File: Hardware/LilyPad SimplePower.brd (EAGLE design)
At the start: 27.9 x 27.9 mm, 20 parts, among them U1 MCP73831

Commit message: Adding review changes
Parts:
- added U$6: REVISION, SparkFun-Aesthetics:REVISION
- SJ1: value SOLDERJUMPERTRACE -> SOLDERJUMPERNC; device SparkFun-Passives:SJ_2S-TRACE -> SparkFun-Passives:SJ_2S
- U$1: value LOGO-LPL -> LOGO-LPLP; device LilyPad-Wearables:LOGO-L -> LilyPad-Wearables:LOGO-LILYPAD
- moved JP3 3.24 mm to (5.71, -4.13)
- moved U$5 3.17 mm to (-6.03, -2.54)
- moved S1 1.80 mm to (0.00, -2.54)
- moved C2 1.42 mm to (-6.35, -13.0)
- moved JP1 1.31 mm to (-9.84, -2.54)
- moved R4 1.27 mm to (-4.45, -13.0)
- moved U1 1.27 mm to (-5.71, -8.89)
- moved U$1 1.27 mm to (-0.64, 2.54), turned to 0 degrees
- moved C1 0.64 mm to (-1.27, -7.62)
- moved R3 0.64 mm to (1.27, -7.62)
- moved JP4 0.32 mm to (12.4, -2.54)
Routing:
- net N$2: track 6.13 -> 8.58 mm
- net N$4: track 16.3 -> 17.5 mm
- net N$5: track 3.41 -> 4.05 mm
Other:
- board size 27.9 x 27.9 mm -> 28.4 x 28.4 mm
- board text added: "NC"

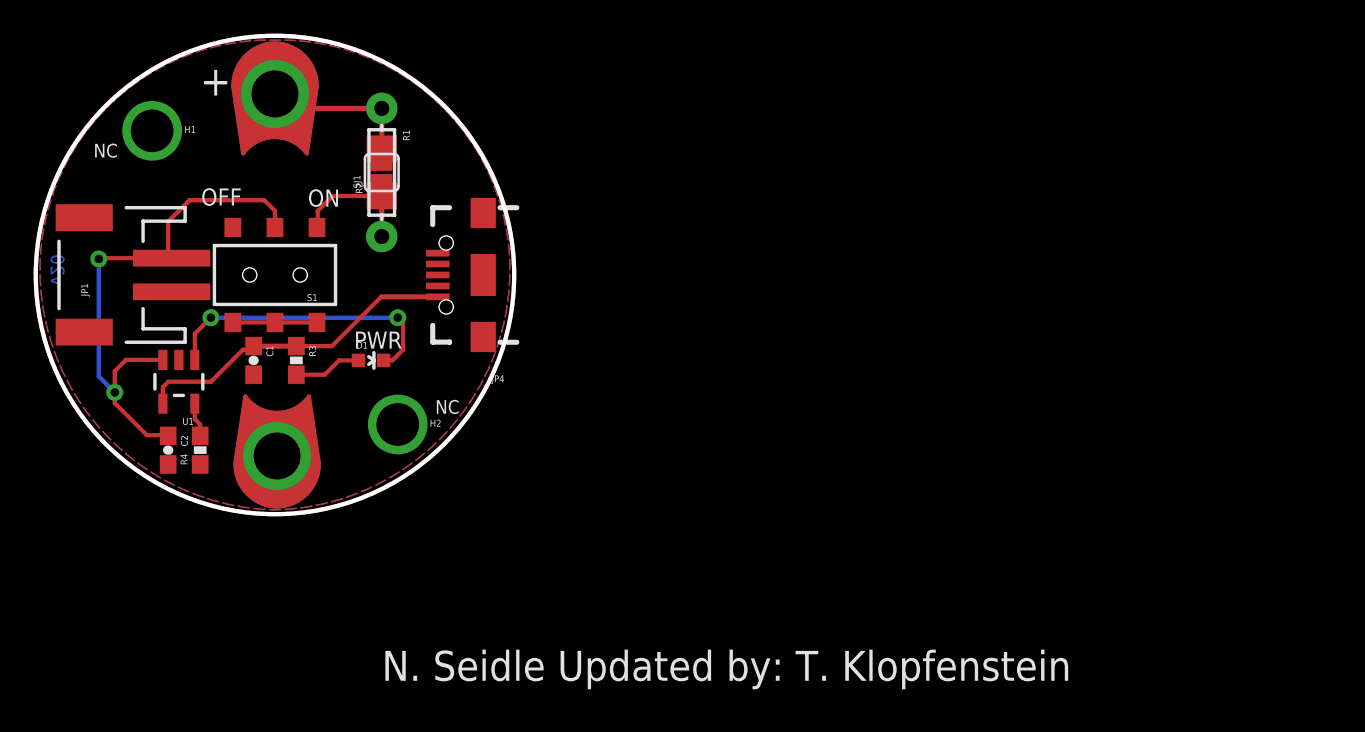
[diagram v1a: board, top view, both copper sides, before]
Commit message: Fixing PWR label to CHG on LED
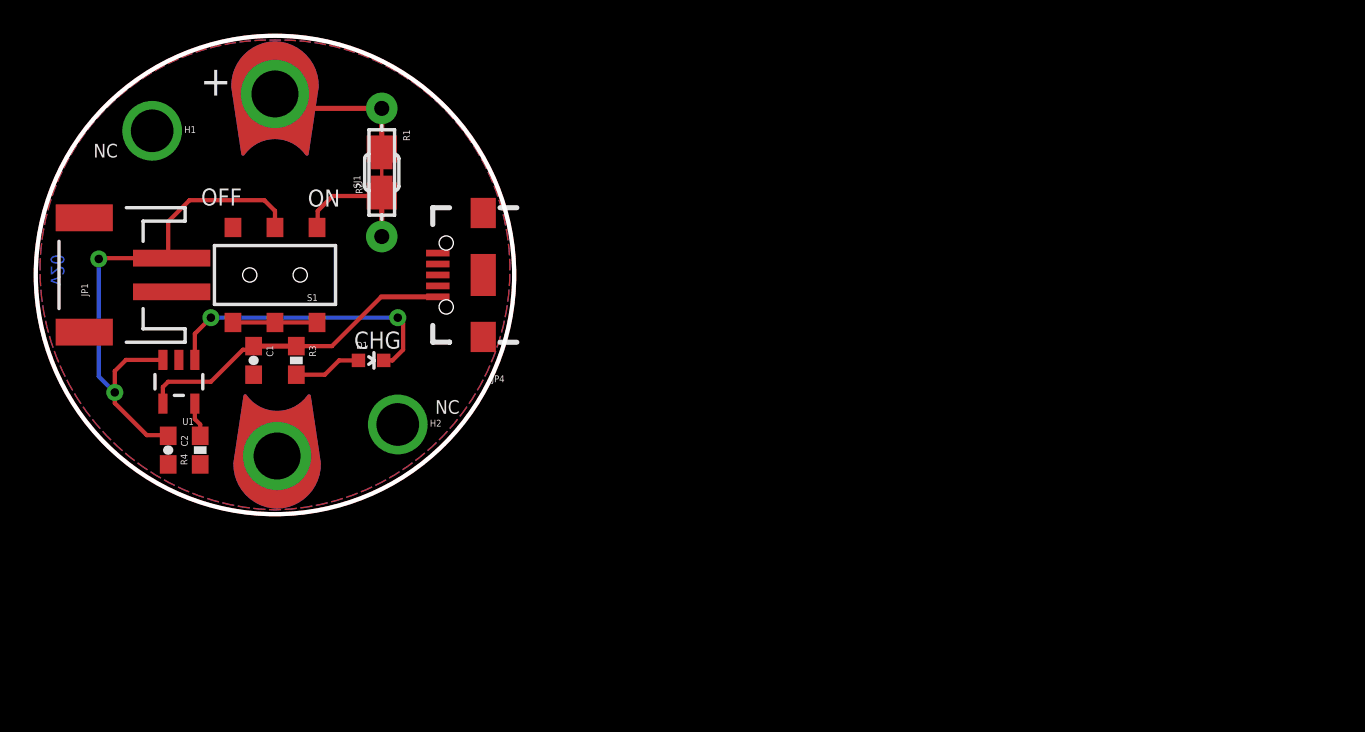
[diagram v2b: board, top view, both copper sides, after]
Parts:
- removed U$2: (no value), SparkFun-Aesthetics:CREATIVE_COMMONS
- added FRAME1: FRAME-LETTER, SparkFun-Aesthetics:CREATIVE_COMMONS
- SJ1: value SOLDERJUMPERNC -> SOLDERJUMPERTRACE; device SparkFun-Passives:SJ_2S -> SparkFun-Passives:SJ_2S-TRACE
- moved U$6 31.8 mm to (-12.7, -29.2)
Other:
- board text added: "CHG"
- board text added: "N. Seidle"
- board text added: "Toni Klopfenstein"
- board text removed: "N. Seidle Updated by: T. Klopfenstein"
- board text removed: "PWR"

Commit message: midway work  on updating design
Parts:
- removed R1: (no value), SparkFun:AXIAL-0.3
- removed R2: (no value), SparkFun:1206
- removed SJ1: SOLDERJUMPERTRACE, SparkFun-Passives:SJ_2S-TRACE
- added H3, H4: SEW_HOLE, LilyPad-Wearables:SIMPLE_HOLE
- moved H2 16.9 mm to (9.21, 5.40)
- moved C2 15.9 mm to (-1.65, 2.22), turned to 0 degrees
- moved U1 7.31 mm to (-1.59, -2.86)
- moved R4 7.17 mm to (-1.65, -6.35), turned to 0 degrees
- moved C1 4.80 mm to (-6.03, -8.26), turned to 180 degrees
- moved S1 4.13 mm to (4.13, -2.54), turned to 270 degrees
- moved R3 2.93 mm to (-1.59, -8.26), turned to 0 degrees
- moved D1 2.01 mm to (3.81, -8.26)
- moved H1 1.71 mm to (-8.89, 5.40)
- moved U$1 1.00 mm to (0.32, 2.22)
- moved JP1 0.32 mm to (-9.84, -2.86)
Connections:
- removed net +: R1.P$1, R2.2, SJ1.2, U$4.1
- removed net N$2: R1.P$2, R2.1, S1.4, SJ1.1
- removed net SINK2: S1.6
- new net N$6: S1.4, U$4.1
- net GND: now also S1.6
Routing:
- net N$1: track 32.1 -> 14.1 mm, vias 2 -> 0
- net +: track 10.0 -> 0.00 mm
- net N$6: track 0.00 -> 8.80 mm
- net N$2: track 8.48 -> 0.00 mm
- net N$4: track 17.5 -> 10.3 mm, vias 2 -> 0
- net N$3: track 19.6 -> 23.1 mm, vias 0 -> 2
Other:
- board text added: "-"

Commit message: More petal work
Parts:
- H1: value SEW_HOLE -> SEWTAP4; device LilyPad-Wearables:SIMPLE_HOLE -> LilyPad-Wearables:PETAL-SMALL
- H2, H3, H4: value SEW_HOLE -> SEWTAP6; device LilyPad-Wearables:SIMPLE_HOLE -> LilyPad-Wearables:PETAL-SMALL-2SIDE
- moved D1 2.31 mm to (1.59, -7.62), turned to 0 degrees
- moved C1 1.14 mm to (-6.99, -7.62)
- moved H3 1.14 mm to (8.57, -11.1), turned to 45 degrees
- moved H4 1.14 mm to (-8.57, -11.1), turned to 315 degrees
- moved H2 0.90 mm to (8.57, 6.03), turned to 135 degrees
- moved H1 0.71 mm to (-8.57, 6.03), turned to 225 degrees
- moved R3 0.64 mm to (-1.59, -7.62)
- moved R4 0.63 mm to (-1.65, -5.71)
- moved JP1 0.32 mm to (-9.84, -2.54)
- moved U1 0.32 mm to (-1.59, -2.54)
- moved U$3 0.17 mm to (-0.04, -13.4)
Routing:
- net N$3: track 23.1 -> 27.3 mm
- net N$5: track 3.80 -> 2.64 mm
- net N$4: track 10.3 -> 9.35 mm
- net N$1: track 14.1 -> 13.6 mm

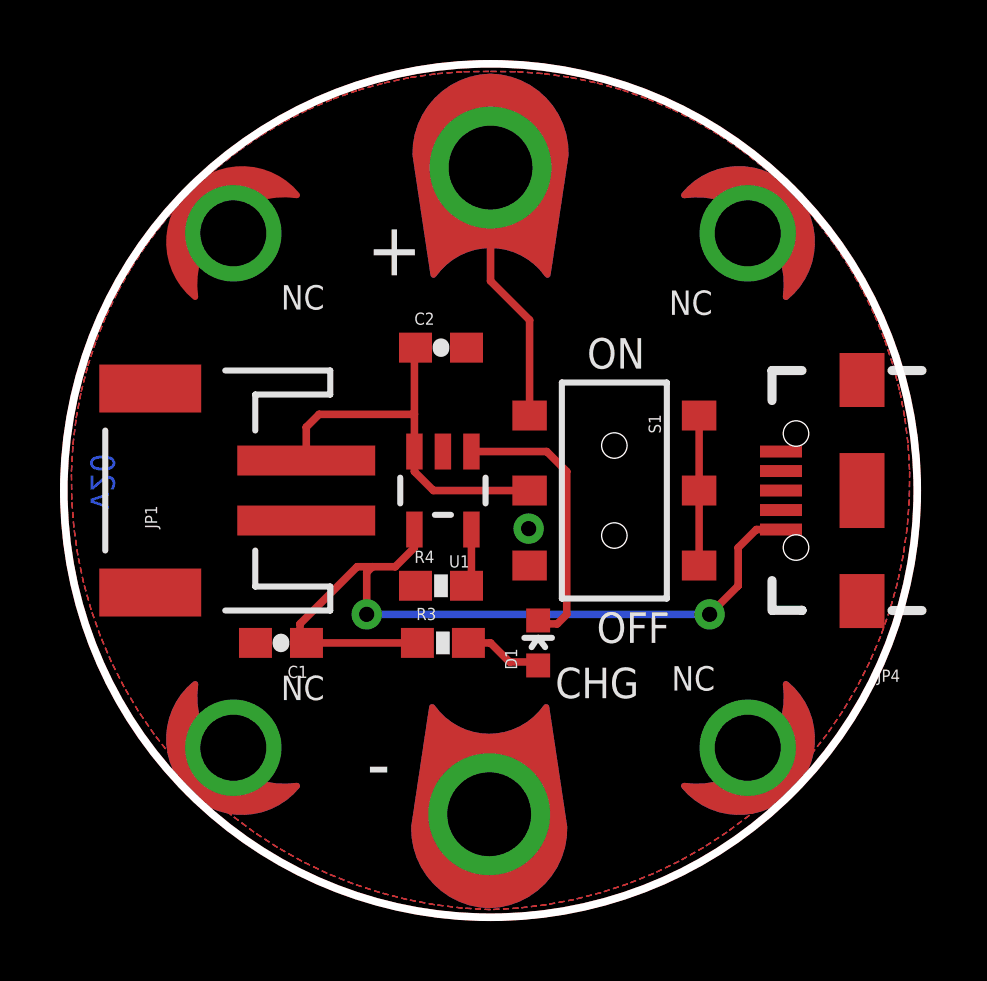
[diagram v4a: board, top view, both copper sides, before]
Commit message: Initial polygon pours corrected
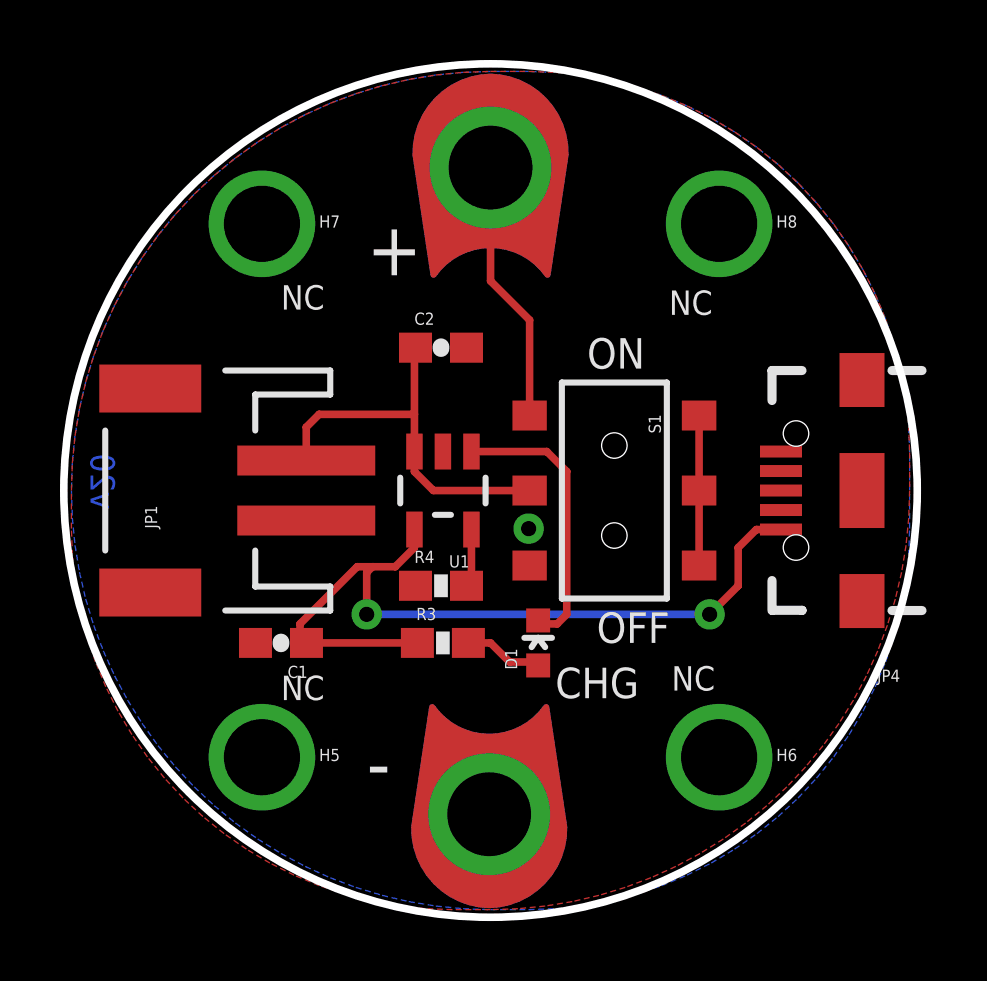
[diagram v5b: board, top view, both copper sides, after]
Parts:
- removed H1: SEWTAP4, LilyPad-Wearables:PETAL-SMALL
- removed H2, H3, H4: SEWTAP6, LilyPad-Wearables:PETAL-SMALL-2SIDE
- added H5, H6, H7, H8: SEW_HOLE, LilyPad-Wearables:SIMPLE_HOLE
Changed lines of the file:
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@@
 <setting verticaltext="up"/>
 </settings>
-<grid distance="0.0125" unitdist="inch" unit="inch" style="lines" multiple="1" display="yes" altdistance="0.005" altunitdist="inch" altunit="inch"/>
+<grid distance="0.05" unitdist="inch" unit="inch" style="lines" multiple="1" display="yes" altdistance="0.005" altunitdist="inch" altunit="inch"/>
 <layers>
 <layer number="1" name="Top" color="4" fill="1" visible="yes" active="yes"/>
@@
 <layer number="27" name="tValues" color="7" fill="1" visible="no" active="yes"/>
 <layer number="28" name="bValues" color="7" fill="1" visible="no" active="yes"/>
-<layer number="29" name="tStop" color="13" fill="3" visible="yes" active="yes"/>
-<layer number="30" name="bStop" color="7" fill="6" visible="yes" active="yes"/>
+<layer number="29" name="tStop" color="13" fill="3" visible="no" active="yes"/>
+<layer number="30" name="bStop" color="7" fill="6" visible="no" active="yes"/>
 <layer number="31" name="tCream" color="7" fill="4" visible="no" active="yes"/>
 <layer number="32" name="bCream" color="7" fill="5" visible="no" active="yes"/>
@@
 <layer number="45" name="Holes" color="7" fill="1" visible="yes" active="yes"/>
 <layer number="46" name="Milling" color="3" fill="1" visible="no" active="yes"/>
-<layer number="47" name="Measures" color="7" fill="1" visible="yes" active="yes"/>
+<layer number="47" name="Measures" color="7" fill="1" visible="no" active="yes"/>
 <layer number="48" name="Document" color="7" fill="1" visible="no" active="yes"/>
-<layer number="49" name="Reference" color="7" fill="1" visible="no" active="yes"/>
+<layer number="49" name="Reference" color="7" fill="1" visible="yes" active="yes"/>
 <layer number="50" name="dxf" color="7" fill="1" visible="no" active="yes"/>
 <layer number="51" name="tDocu" color="6" fill="1" visible="yes" active="yes"/>
@@
 <text x="-13.335" y="-3.175" size="0.8128" layer="16" font="vector" ratio="25" rot="SMR90">v20</text>
 <circle x="0" y="-2.54" radius="14.224" width="0.254" layer="20"/>
-<circle x="0" y="-2.54" radius="14.224" width="0.254" layer="1"/>
-<circle x="0" y="-2.54" radius="14.224" width="0.254" layer="23"/>
 <text x="2.159" y="-9.4615" size="1.016" layer="21" font="vector" ratio="15">CHG</text>
 <text x="-6.985" y="3.4925" size="0.8128" layer="21" font="vector" ratio="15">NC</text>
@@
 <text x="-6.985" y="-9.525" size="0.8128" layer="21" font="vector" ratio="15">NC</text>
 <text x="-4.1275" y="-12.5095" size="1.778" layer="21" font="vector" ratio="15">-</text>
-<circle x="0" y="-2.54" radius="12.7" width="2.54" layer="30"/>
 <wire x1="0" y1="12.065" x2="0" y2="-2.54" width="0" layer="47"/>
-<wire x1="0" y1="-2.54" x2="0" y2="-17.78" width="0" layer="47"/>
-<wire x1="-16.51" y1="-2.54" x2="0" y2="-2.54" width="0" layer="47"/>
-<wire x1="0" y1="-2.54" x2="16.51" y2="-2.54" width="0" layer="47"/>
-<wire x1="0" y1="-2.54" x2="-11.43" y2="-13.97" width="0" layer="47"/>
-<wire x1="0" y1="-2.54" x2="10.795" y2="8.255" width="0" layer="47"/>
-<wire x1="0" y1="-2.54" x2="-11.43" y2="8.89" width="0" layer="47"/>
-<wire x1="0" y1="-2.54" x2="11.43" y2="-13.97" width="0" layer="47"/>
-<wire x1="-6.35" y1="7.3025" x2="-2.8575" y2="8.5725" width="0.254" layer="29" curve="-116.29479"/>
-<wire x1="2.8575" y1="8.255" x2="6.35" y2="7.3025" width="0.254" layer="29" curve="-158.198591"/>
-<wire x1="10.16" y1="3.81" x2="11.43" y2="2.2225" width="0.254" layer="29" curve="-180"/>
+<circle x="0" y="-2.54" radius="14.19903125" width="0.254" layer="30"/>
+<circle x="0" y="-2.54" radius="11.811" width="5.08" layer="42"/>
 </plain>
 <attributes>
@@
 <element name="U$6" library="SparkFun-Aesthetics" package="REVISION" value="REVISION" x="-12.7" y="-29.21"/>
 <element name="FRAME1" library="SparkFun-Aesthetics" package="CREATIVE_COMMONS" value="FRAME-LETTER" x="-24.237121875" y="-26.797"/>
-<element name="H1" library="LilyPad-Wearables" package="PETAL-SMALL" value="SEWTAP4" x="-8.5725" y="6.0325" rot="R225"/>
-<element name="H2" library="LilyPad-Wearables" package="PETAL-SMALL-2SIDE" value="SEWTAP6" x="8.5725" y="6.0325" rot="R135"/>
-<element name="H3" library="LilyPad-Wearables" package="PETAL-SMALL-2SIDE" value="SEWTAP6" x="8.5725" y="-11.1125" rot="R45"/>
-<element name="H4" library="LilyPad-Wearables" package="PETAL-SMALL-2SIDE" value="SEWTAP6" x="-8.5725" y="-11.1125" rot="R315"/>
+<element name="H5" library="LilyPad-Wearables" package="SIMPLE_HOLE" value="SEW_HOLE" x="-7.62" y="-11.43"/>
+<element name="H6" library="LilyPad-Wearables" package="SIMPLE_HOLE" value="SEW_HOLE" x="7.62" y="-11.43"/>
+<element name="H7" library="LilyPad-Wearables" package="SIMPLE_HOLE" value="SEW_HOLE" x="-7.62" y="6.35"/>
+<element name="H8" library="LilyPad-Wearables" package="SIMPLE_HOLE" value="SEW_HOLE" x="7.62" y="6.35"/>
 </elements>
 <signals>
@@
 <contactref element="C2" pad="2"/>
 <contactref element="R4" pad="1"/>
-<polygon width="0.254" layer="1" isolate="0.3048">
-<vertex x="-13.97" y="-1.905" curve="-90"/>
-<vertex x="0" y="11.43" curve="-90"/>
-<vertex x="13.97" y="-1.905" curve="-90"/>
-<vertex x="0" y="-16.51" curve="-90"/>
+<contactref element="S1" pad="6"/>
+<via x="1.27" y="-3.81" extent="1-16" drill="0.508"/>
+<polygon width="0.254" layer="16">
+<vertex x="-13.97" y="-2.54" curve="90"/>
+<vertex x="0" y="-16.51"/>
+<vertex x="1.27" y="-16.51" curve="90"/>
+<vertex x="13.97" y="-3.81"/>
+<vertex x="13.97" y="-1.27" curve="90"/>
+<vertex x="1.27" y="11.43"/>
+<vertex x="0" y="11.43" curve="90"/>
 </polygon>
-<polygon width="0.254" layer="16" isolate="0.3048">
-<vertex x="-13.97" y="-1.905" curve="-90"/>
-<vertex x="0" y="11.43" curve="-90"/>
-<vertex x="13.97" y="-1.905" curve="-90"/>
-<vertex x="0" y="-16.51" curve="-90"/>
+<polygon width="0.254" layer="1">
+<vertex x="-13.97" y="-2.54" curve="-90"/>
+<vertex x="0" y="11.43"/>
+<vertex x="1.27" y="11.43" curve="-90"/>
+<vertex x="13.97" y="-1.27"/>
+<vertex x="13.97" y="-2.54" curve="-90"/>
+<vertex x="0" y="-16.51"/>
+<vertex x="-1.27" y="-16.51" curve="-90"/>
+<vertex x="-13.97" y="-3.81"/>
 </polygon>
-<contactref element="S1" pad="6"/>
-<polygon width="0.254" layer="1" isolate="0.3048">
-<vertex x="-13.97" y="-1.905" curve="-90"/>
-<vertex x="0" y="11.43" curve="-90"/>
-<vertex x="13.97" y="-1.905" curve="-90"/>
-<vertex x="0" y="-16.51" curve="-90"/>
-</polygon>
-<via x="1.27" y="-3.81" extent="1-16" drill="0.508"/>
 </signal>
 <signal name="N$1">
